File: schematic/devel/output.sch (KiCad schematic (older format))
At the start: 37 parts

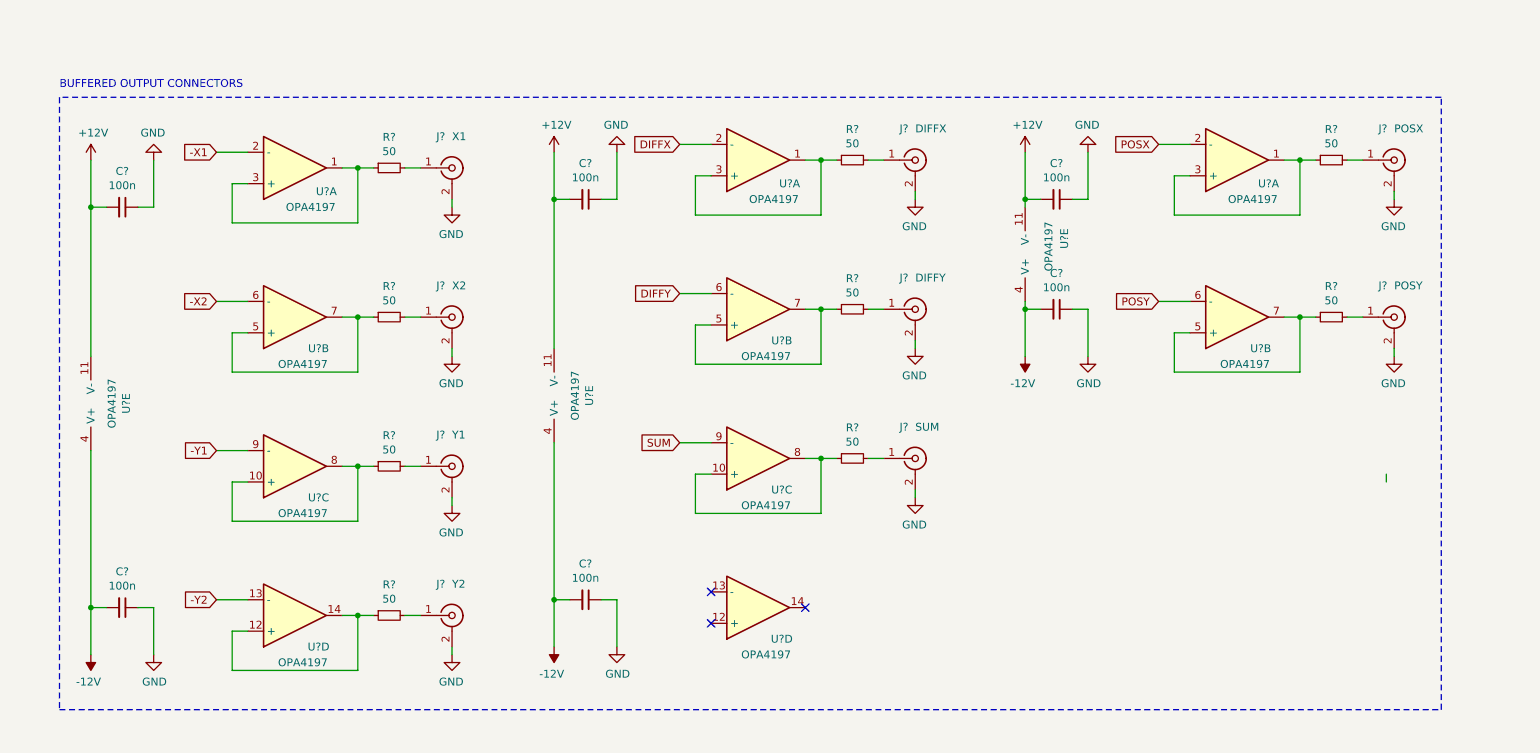
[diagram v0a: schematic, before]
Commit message: fixed opamp supply voltage polarisation, fixed output buffers
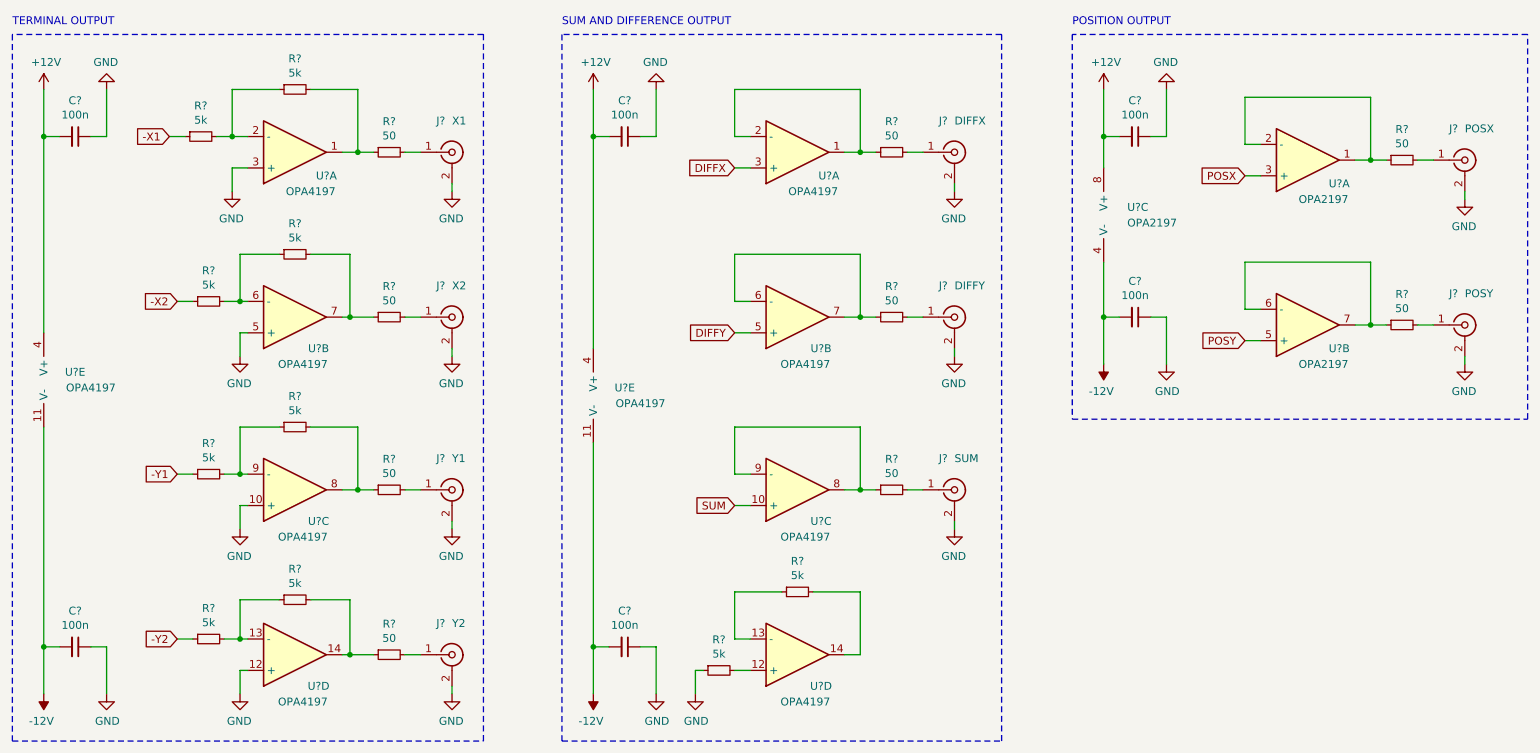
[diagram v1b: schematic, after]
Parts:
- removed J?: POSX, symbol Connector:Conn_Coaxial
- removed J?: POSY, symbol Connector:Conn_Coaxial
- removed R? (x2): 50, symbol Device:R_Small
- removed U? (x3): OPA4197, symbol Device:Opamp_Quad_Generic
- added J?: POSX, symbol Connector:Conn_Coaxial
- added J?: POSY, symbol Connector:Conn_Coaxial
- added R? (x10): 5k, symbol Device:R_Small
- added R? (x2): 50, symbol Device:R_Small
- added U? (x3): OPA2197, symbol Device:Opamp_Dual_Generic
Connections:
- net +12V: now also U?.4 (V+), U?.4 (V+), U?.8 (V+); no longer U?.11 (V-), U?.11 (V-)
- net -12V: now also U?.11 (V-), U?.11 (V-), U?.4 (V-); no longer U?.4 (V+), U?.4 (V+)
- net -X1: now also R?.1; no longer U?.2 (-)
- net -X2: now also R?.1; no longer U?.6 (-)
- net -Y1: now also R?.1; no longer U?.9 (-)
- net -Y2: now also R?.1; no longer U?.13 (-)
- net DIFFX: now also U?.3 (+); no longer U?.2 (-)
- net DIFFY: now also U?.5 (+); no longer U?.6 (-)
- net GND: now also U?.10 (+), U?.12 (+), U?.3 (+), U?.5 (+), J?.2 (Ext), J?.2 (Ext), R?.1
- net POSX: now also U?.3 (+)
- net POSY: now also U?.5 (+)
- net SUM: now also U?.10 (+); no longer U?.9 (-)
- net at R?.1, U?.1: now also R?.2; no longer U?.3 (+)
- net at R?.1, U?.7: now also R?.2; no longer U?.5 (+)
- net at R?.1, U?.8: now also R?.2; no longer U?.10 (+)
- net at R?.1, U?.14: now also R?.2; no longer U?.12 (+)
- net at R?.1, U?.1: now also U?.2 (-); no longer U?.3 (+)
- net at R?.1, U?.7: now also U?.6 (-); no longer U?.5 (+)
- net at R?.1, U?.8: now also U?.9 (-); no longer U?.10 (+)
- net at U?.12 (+): now also R?.2
- net at U?.13 (-): now also R?.1
- net at U?.14: now also R?.2
- new net: R?.1, U?.1, U?.2 (-)
- new net: R?.1, U?.6 (-), U?.7
- new net: R?.1, R?.2, U?.2 (-)
- new net: R?.1, R?.2, U?.6 (-)
- new net: R?.1, R?.2, U?.9 (-)
- new net: R?.1, R?.2, U?.13 (-)
- new net: J?.1 (In), R?.2 (x2)
- no-connect marks 3 -> 0
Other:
- note added: "POSITION OUTPUT"
- note added: "SUM AND DIFFERENCE OUTPUT"
- note added: "TERMINAL OUTPUT"
- note removed: "BUFFERED OUTPUT CONNECTORS"
- moved on the sheet: C?, J?, R?, U?A, U?B, U?C, U?D, U?E

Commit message: fixed floating buffer in arthimetic unit
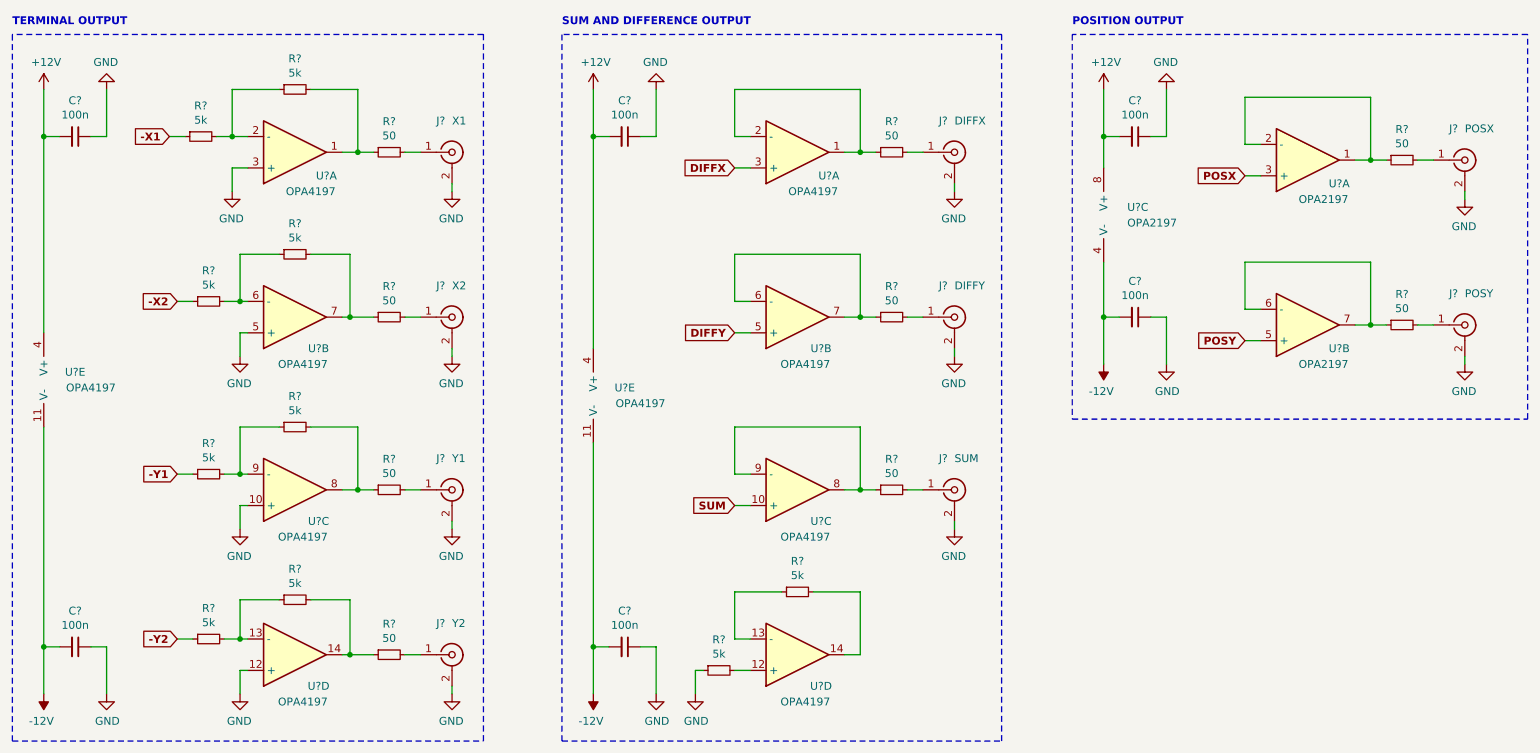
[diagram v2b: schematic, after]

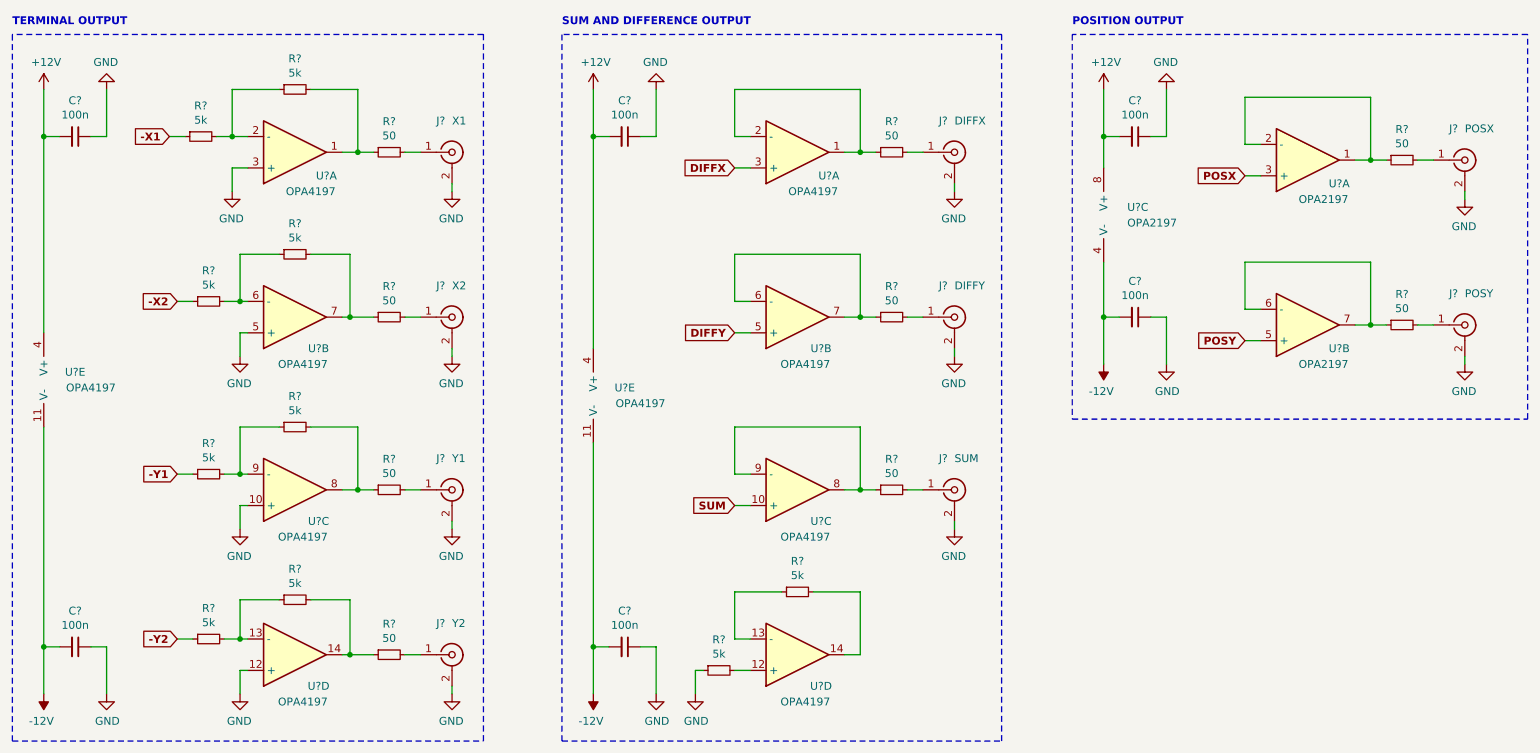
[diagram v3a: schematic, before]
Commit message: removed arithmetic unit from development board, changed output connectors
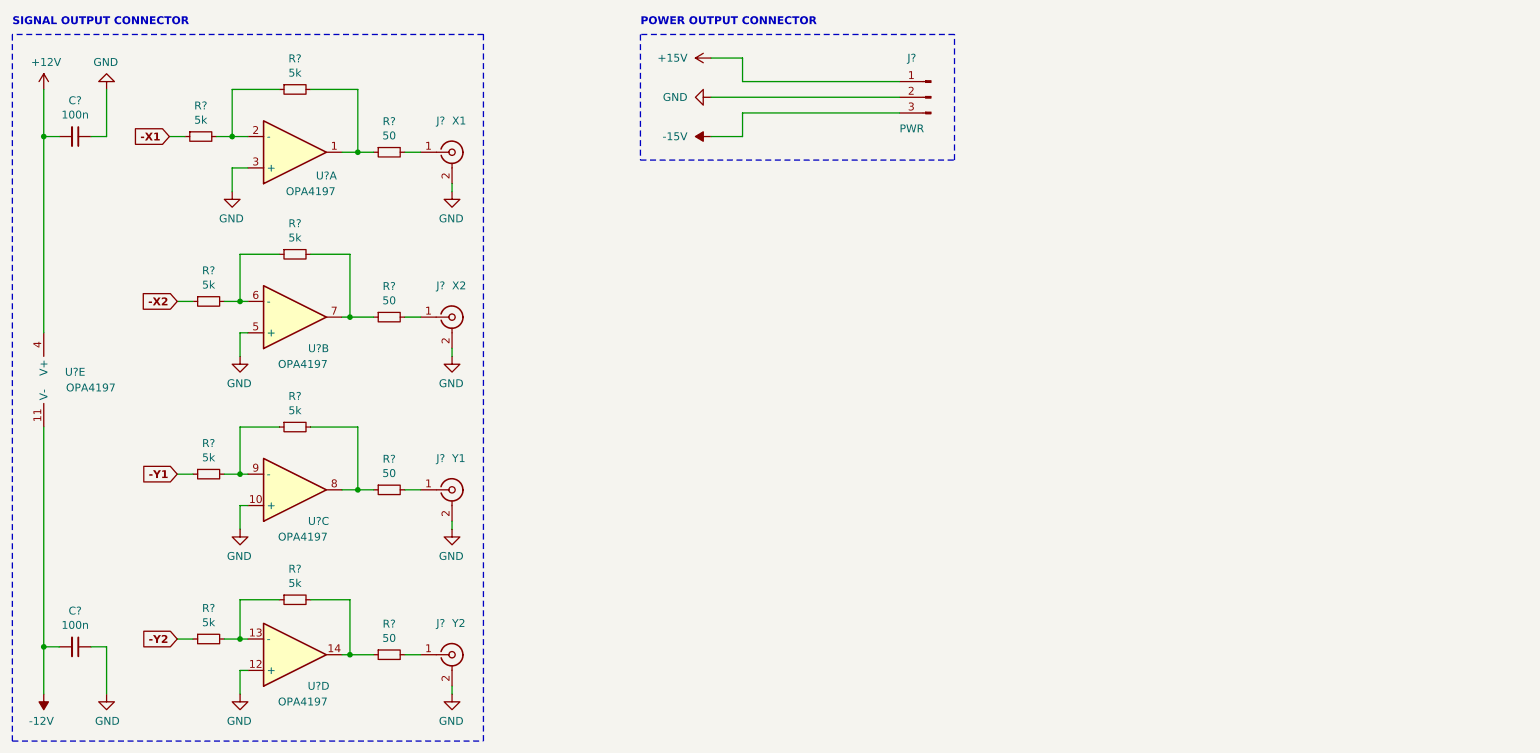
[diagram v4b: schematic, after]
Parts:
- removed C? (x4): 100n, symbol Device:C_Small
- removed J?: POSX, symbol Connector:Conn_Coaxial
- removed J?: POSY, symbol Connector:Conn_Coaxial
- removed J?: DIFFX, symbol Connector:Conn_Coaxial
- removed J?: DIFFY, symbol Connector:Conn_Coaxial
- removed J?: SUM, symbol Connector:Conn_Coaxial
- removed R? (x2): 5k, symbol Device:R_Small
- removed R? (x5): 50, symbol Device:R_Small
- removed U? (x3): OPA2197, symbol Device:Opamp_Dual_Generic
- removed U? (x5): OPA4197, symbol Device:Opamp_Quad_Generic
- added J?: PWR, symbol Connector:Conn_01x03_Male
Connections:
- net GND: now also J?.2 (Pin_2)
- new net +15V: J?.1 (Pin_1)
- new net -15V: J?.3 (Pin_3)
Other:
- note added: "POWER OUTPUT CONNECTOR"
- note added: "SIGNAL OUTPUT CONNECTOR"
- note removed: "POSITION OUTPUT"
- note removed: "SUM AND DIFFERENCE OUTPUT"
- note removed: "TERMINAL OUTPUT"

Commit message: made small adjustments, created netlist
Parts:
- J2: renamed from J?; value X1 -> CONN_X1
- J3: renamed from J?; value X2 -> CONN_X2
- J4: renamed from J?; value Y1 -> CONN_Y1
- J5: renamed from J?; value Y2 -> CONN_Y2
- J6: renamed from J?; value PWR -> CONN_PWR
- gave numbers to parts that had none: 15

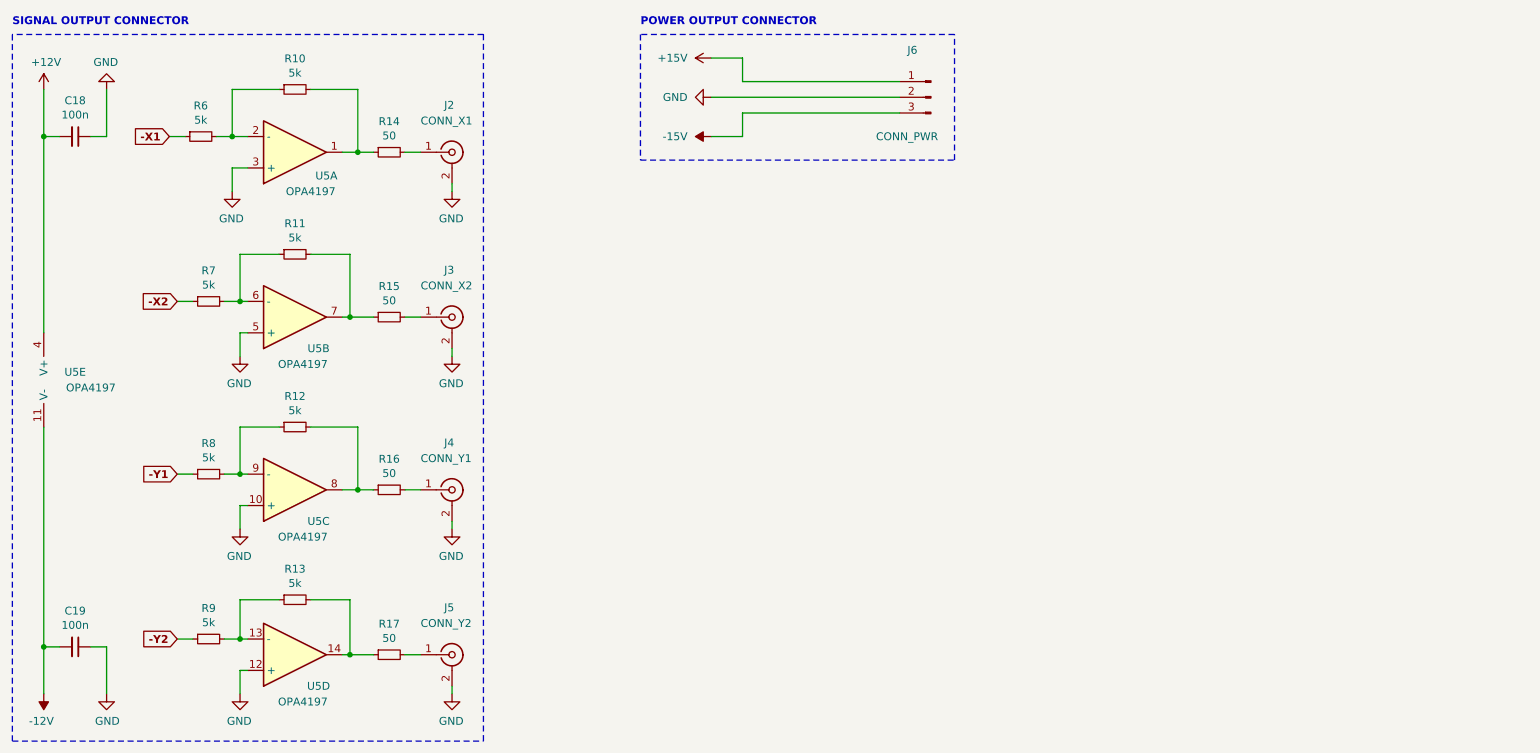
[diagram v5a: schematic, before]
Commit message: removed inverting output opamps
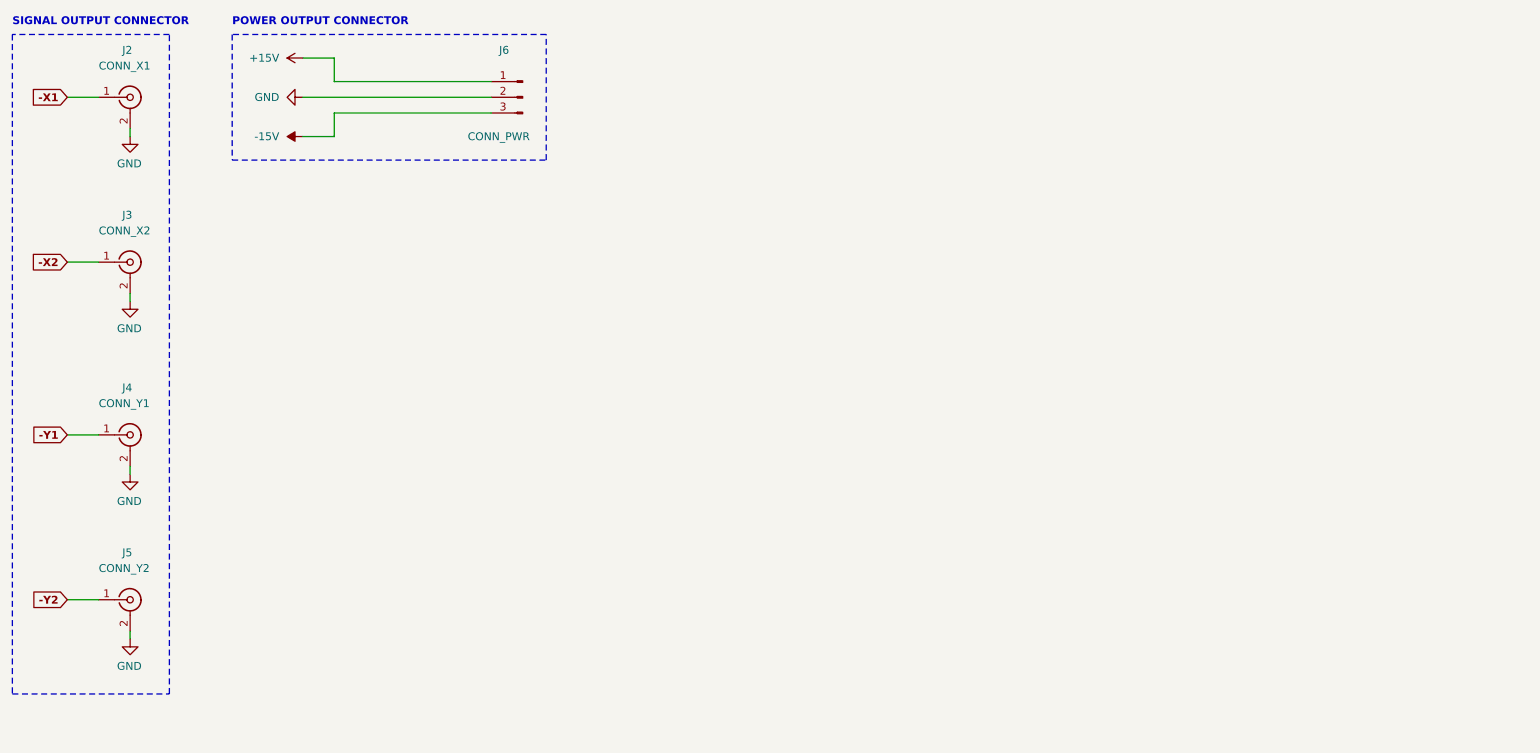
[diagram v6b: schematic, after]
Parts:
- removed C18, C19: 100n, symbol Device:C_Small
- removed R10, R11, R12, R13, R6, R7, R8, R9: 5k, symbol Device:R_Small
- removed R14, R15, R16, R17: 50, symbol Device:R_Small
- removed U5: OPA4197, symbol Device:Opamp_Quad_Generic
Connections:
- net -X1: now also J2.1 (In)
- net -X2: now also J3.1 (In)
- net -Y1: now also J4.1 (In)
- net -Y2: now also J5.1 (In)
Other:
- moved on the sheet: J2, J3, J4, J5, J6

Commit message: assigned footprints to symbols
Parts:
- J2, J3, J4, J5: footprint (none) -> Connector_Coaxial:SMA_Amphenol_901-144_Vertical
- J6: footprint (none) -> Connector_PinHeader_1.00mm:PinHeader_1x03_P1.00mm_Vertical
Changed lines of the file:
@@
 F 0 "J5" H 1700 5400 50  0000 L CNN
 F 1 "CONN_Y2" H 1550 5300 50  0000 L CNN
-F 2 "" H 1750 5100 50  0001 C CNN
+F 2 "Connector_Coaxial:SMA_Amphenol_901-144_Vertical" H 1750 5100 50  0001 C CNN
 F 3 " ~" H 1750 5100 50  0001 C CNN
 	1    1750 5100
@@
 F 0 "J4" H 1700 4350 50  0000 L CNN
 F 1 "CONN_Y1" H 1550 4250 50  0000 L CNN
-F 2 "" H 1750 4050 50  0001 C CNN
+F 2 "Connector_Coaxial:SMA_Amphenol_901-144_Vertical" H 1750 4050 50  0001 C CNN
 F 3 " ~" H 1750 4050 50  0001 C CNN
 	1    1750 4050
@@
 F 0 "J3" H 1700 3250 50  0000 L CNN
 F 1 "CONN_X2" H 1550 3150 50  0000 L CNN
-F 2 "" H 1750 2950 50  0001 C CNN
+F 2 "Connector_Coaxial:SMA_Amphenol_901-144_Vertical" H 1750 2950 50  0001 C CNN
 F 3 " ~" H 1750 2950 50  0001 C CNN
 	1    1750 2950
@@
 F 0 "J2" H 1700 2200 50  0000 L CNN
 F 1 "CONN_X1" H 1550 2100 50  0000 L CNN
-F 2 "" H 1750 1900 50  0001 C CNN
+F 2 "Connector_Coaxial:SMA_Amphenol_901-144_Vertical" H 1750 1900 50  0001 C CNN
 F 3 " ~" H 1750 1900 50  0001 C CNN
 	1    1750 1900
@@
 F 0 "J6" H 4400 2200 50  0000 R CNN
 F 1 "CONN_PWR" H 4600 1650 50  0000 R CNN
-F 2 "" H 4250 1900 50  0001 C CNN
+F 2 "Connector_PinHeader_1.00mm:PinHeader_1x03_P1.00mm_Vertical" H 4250 1900 50  0001 C CNN
 F 3 "~" H 4250 1900 50  0001 C CNN
 	1    4250 1900
